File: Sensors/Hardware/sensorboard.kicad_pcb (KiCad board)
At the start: 4 copper layers, 120 x 50 mm, 302 parts, among them J1 RBUS, J10 1053131104, J11 1053131104, J12 1053131104, J13 1053131104, J14 1053131104, J15 USB_C_Receptacle_USB2.0, J16 Micro_SD_Card_Det, J2 Conn_Coaxial, J3 1053131104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

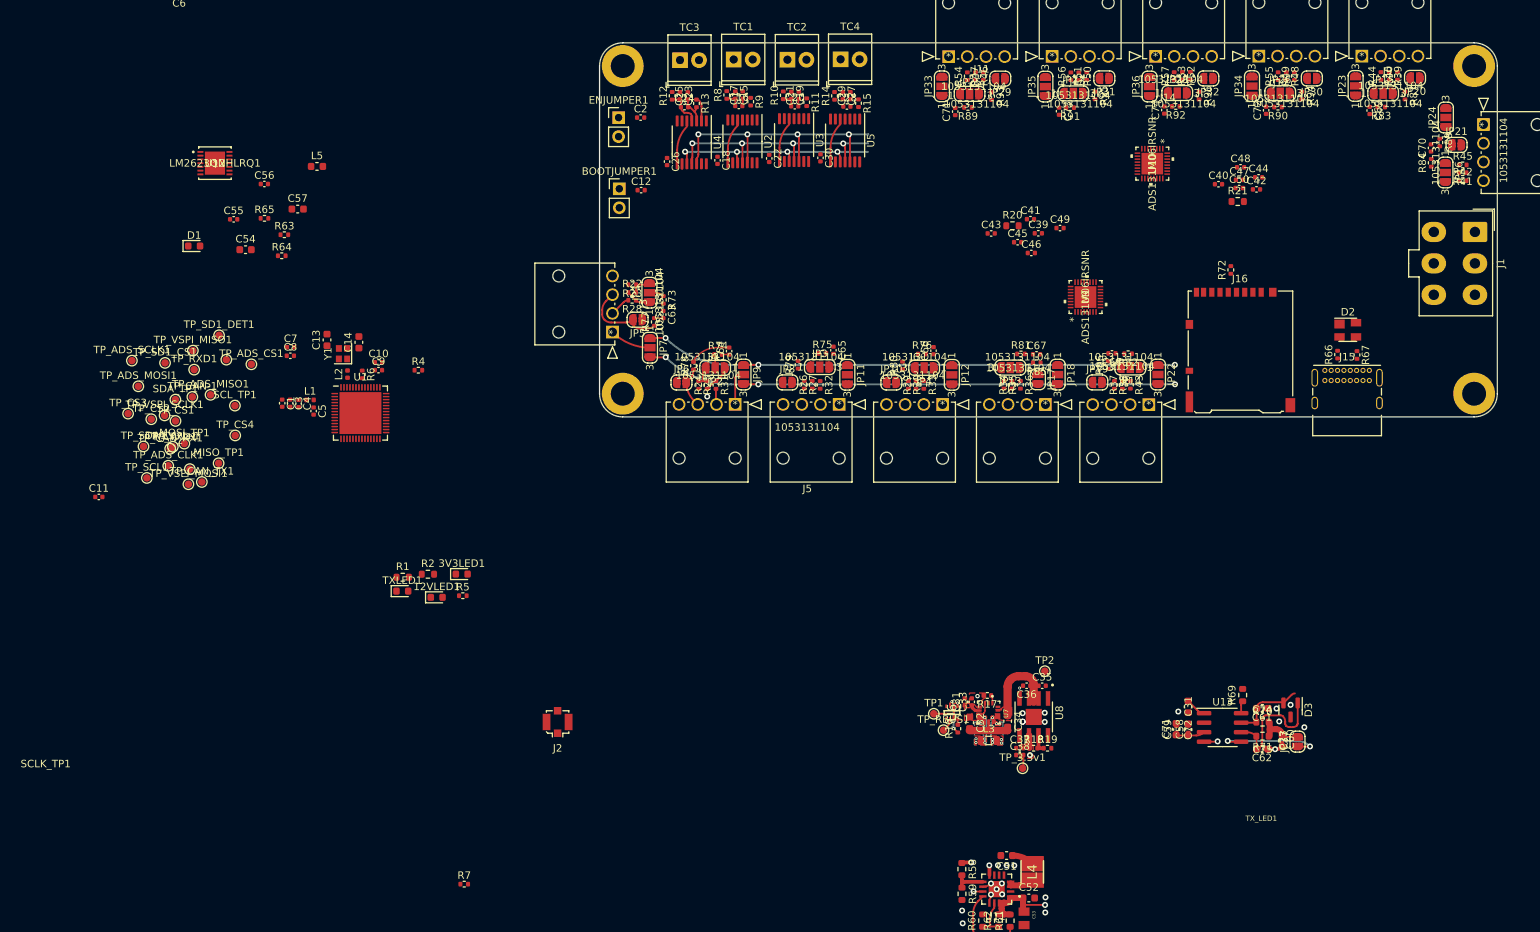
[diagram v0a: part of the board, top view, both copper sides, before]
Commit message: 10v rail layout, adc update
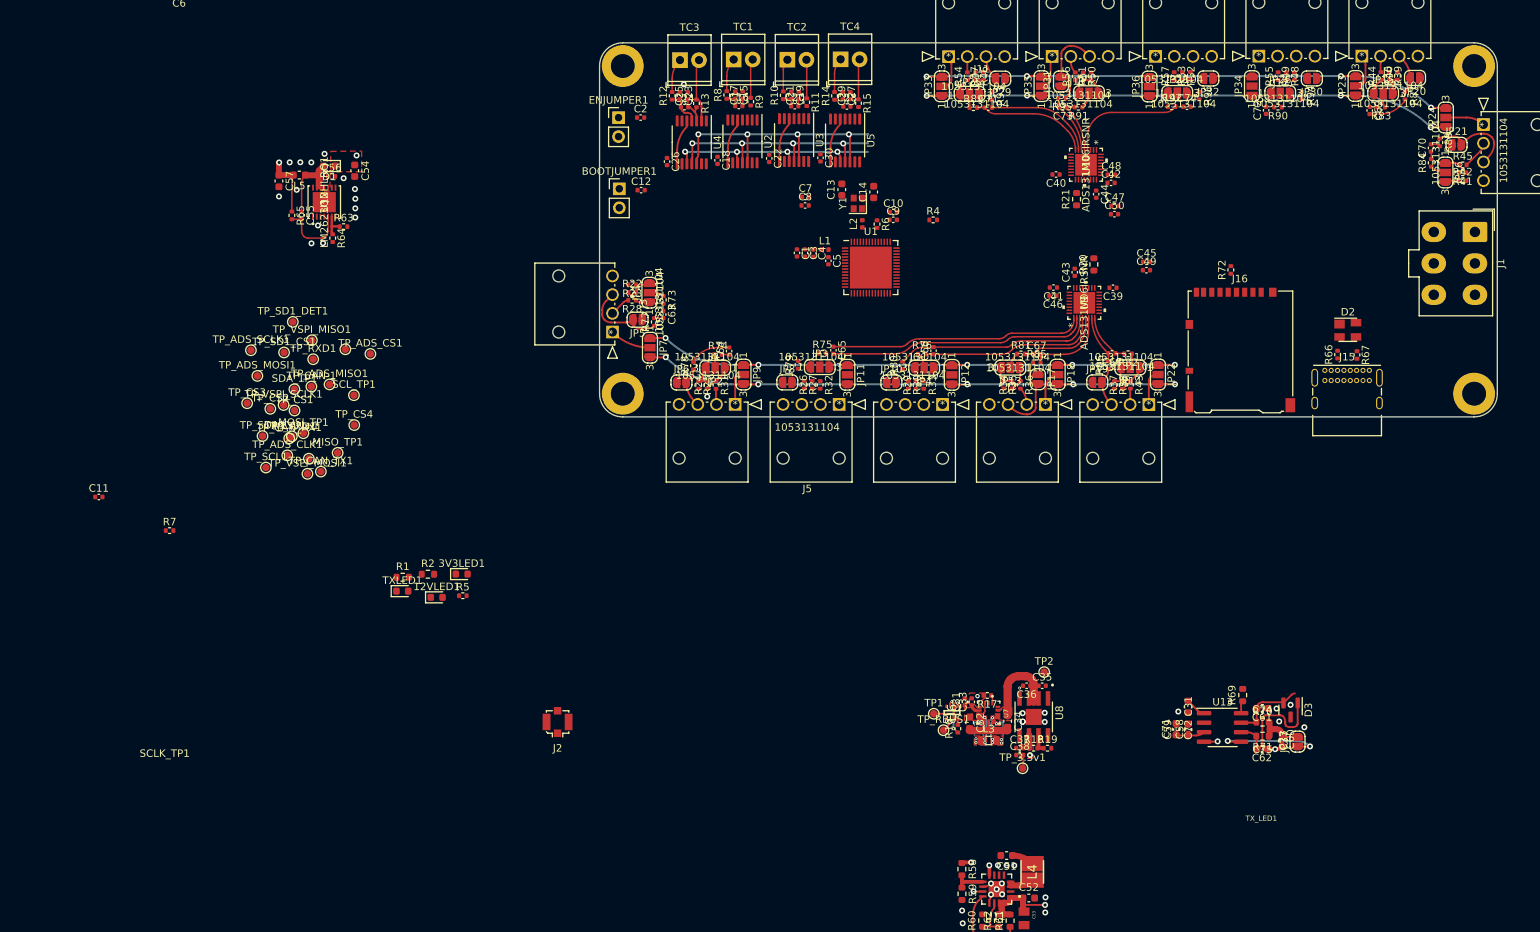
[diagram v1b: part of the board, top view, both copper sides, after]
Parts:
- moved C1 71.7 mm to (106.4, 58.1)
- moved C10 71.7 mm to (119.3, 52.6)
- moved C13 71.7 mm to (112.4, 49.6)
- moved C14 71.7 mm to (116.6, 49.9)
- moved C3 71.7 mm to (107.5, 58.1)
- moved C4 71.7 mm to (108.6, 58.1)
- moved C5 71.7 mm to (110.6, 59.1)
- moved C7 71.7 mm to (107.5, 50.6)
- moved C8 71.7 mm to (107.5, 51.7)
- moved C9 71.7 mm to (119.3, 53.7)
- moved L1 71.7 mm to (110.1, 57.6)
- moved L2 71.7 mm to (115.1, 54.2)
- moved R4 71.7 mm to (124.6, 53.7)
- moved R6 71.7 mm to (117.1, 54.2)
- moved Y1 71.7 mm to (114.5, 51.5)
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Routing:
- net +3V3: track 110.8 -> 202.1 mm, vias 7 -> 14
- net +5V: track 84.8 -> 167.7 mm, vias 4 -> 10
- net /analogueSPI/AIN2N: track 0.00 -> 34.8 mm
- net /analogueSPI/AIN2P: track 0.00 -> 33.9 mm
- net /analogueSPI/AIN3N: track 0.00 -> 26.8 mm
- net /analogueSPI/AIN3P: track 0.00 -> 23.9 mm
- net /analogueSPI/AIN11P: track 0.00 -> 15.8 mm
- net /analogueSPI/AIN11N: track 0.00 -> 15.7 mm
- net /analogueSPI/AIN9P: track 0.00 -> 15.6 mm
- net Net-(J10-Pad3): track 0.00 -> 12.2 mm
- net Net-(J13-Pad3): track 0.00 -> 11.7 mm
- net Net-(J7-Pad3): track 0.00 -> 11.5 mm
- net /analogueSPI/AIN4P: track 0.00 -> 11.4 mm
- net /analogueSPI/AIN4N: track 0.00 -> 11.3 mm
- net Net-(C55-Pad1): track 0.00 -> 9.82 mm
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- added copper zone on F.Cu, net +10V

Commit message: ADC update
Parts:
- moved JP8 5.43 mm to (110.5, 75.0), turned to -90 degrees
- moved JP30 5.38 mm to (169.8, 35.1), turned to 90 degrees
- moved R79 3.93 mm to (110.5, 72.7), turned to 0 degrees
- moved R94 3.80 mm to (170.1, 37.4), turned to 180 degrees
- moved JP3 2.62 mm to (106.8, 73.5), turned to 180 degrees
- moved JP26 2.46 mm to (173.4, 36.7)
- moved R90 1.41 mm to (172.1, 38.5)
- moved R75 1.32 mm to (108.5, 71.6)
- moved JP34 1.24 mm to (166.0, 35.8)
- moved JP11 1.22 mm to (114.3, 74.3)
- moved R26 1.18 mm to (107.2, 75.7)
- moved R27 1.18 mm to (106.2, 75.7)
- moved R32 1.18 mm to (108.3, 75.7)
- moved JP18 1.14 mm to (142.4, 74.4)
- moved C72 1.13 mm to (170.1, 38.4), turned to 180 degrees
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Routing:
- net /analogueSPI/AIN1P: track 0.99 -> 48.0 mm
- net /analogueSPI/AIN1N: track 5.52 -> 52.0 mm
- net /analogueSPI/AIN6P: track 1.01 -> 47.2 mm
- net /analogueSPI/AIN6N: track 1.24 -> 47.3 mm
- net /analogueSPI/AIN7P: track 1.04 -> 38.3 mm
- net /analogueSPI/AIN7N: track 5.46 -> 42.6 mm
- net /analogueSPI/AIN8P: track 0.00 -> 27.2 mm
- net /analogueSPI/AIN8N: track 0.00 -> 26.8 mm
- net /analogueSPI/AIN9N: track 0.00 -> 17.6 mm
- net Net-(J5-Pad3): track 0.00 -> 11.5 mm
- net Net-(J12-Pad3): track 0.00 -> 11.3 mm
- net Net-(J14-Pad3): track 0.00 -> 5.27 mm
- net Net-(J6-Pad3): track 0.00 -> 5.25 mm
- net Net-(J5-Pad1): track 0.00 -> 5.11 mm
- net Net-(J14-Pad1): track 0.00 -> 5.08 mm
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
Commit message: esp32 pin rearrangement
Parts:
- removed J2: Conn_Coaxial, Connector_Coaxial:U.FL_Molex_MCRF_73412-0110_Vertical
- moved C55 116.8 mm to (110.4, 146.3)
- moved C56 116.8 mm to (114.4, 141.2)
- moved R63 116.8 mm to (116.0, 147.9)
- moved R64 116.8 mm to (114.6, 149.4)
- moved R65 116.8 mm to (109.1, 146.4)
- moved U12 116.8 mm to (113.4, 144.6)
- moved C54 116.8 mm to (117.5, 140.4)
- moved C57 116.8 mm to (107.4, 141.8)
- moved D1 116.8 mm to (114.1, 139.8)
- moved L5 116.8 mm to (110.1, 141.0)
- moved C11 108.8 mm to (117.1, 58.7), turned to 90 degrees
- moved C31 100.8 mm to (213.9, 64.0)
- moved C32 100.8 mm to (214.6, 66.8)
- moved C33 100.8 mm to (214.9, 64.0)
- moved C34 100.8 mm to (219.7, 66.6)
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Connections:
- R20 pad 1: +3V3 -> Net-(R20-Pad1)
- R20 pad 2: Net-(R20-Pad2) -> +3V3
- U1 pad 12: /SDA -> unconnected-(U1-Pad12)
- U1 pad 13: /SCL -> unconnected-(U1-Pad13)
- U1 pad 23: /CS2 -> /CAN+
- U1 pad 27: /CS3 -> /CAN_TX
- U1 pad 28: /CS0 -> /CAN_RX
- U1 pad 36: /CAN_TX -> /MOSI
- U1 pad 37: /CAN_RX -> /MISO
- U1 pad 39: /MISO -> /CS2
- U1 pad 40: /SDA -> /CS1
- U1 pad 41: /SCL -> /CS0
- U1 pad 42: /MOSI -> /CS3
- U1 pad 43: /CS1 -> unconnected-(U1-Pad43)
- U1 pad 6: /CAN+ -> unconnected-(U1-Pad6)
- U9 pad 18: Net-(R20-Pad2) -> Net-(R20-Pad1)
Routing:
- net VBUS: track 5.27 -> 18.3 mm
- net /Data-: track 0.00 -> 7.34 mm
- net /Data+: track 0.00 -> 6.76 mm
- net Net-(R68-Pad2): track 0.00 -> 1.26 mm
- net (no net): vias 25 -> 26
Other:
- board text added: "CS regular spi"
- board text added: "Immoveable: DATA +- unavailable pins: 1,4,8,5,2,3,20,30-35,46,52,53,54,56,55,"
- board text added: "POwer circuits just require 3.3V etc. Therefore can be put into the left or right side of the board"
- board text added: "VSPI spi (microSD) CAN TX and RX, CAN +- DAta + and -"

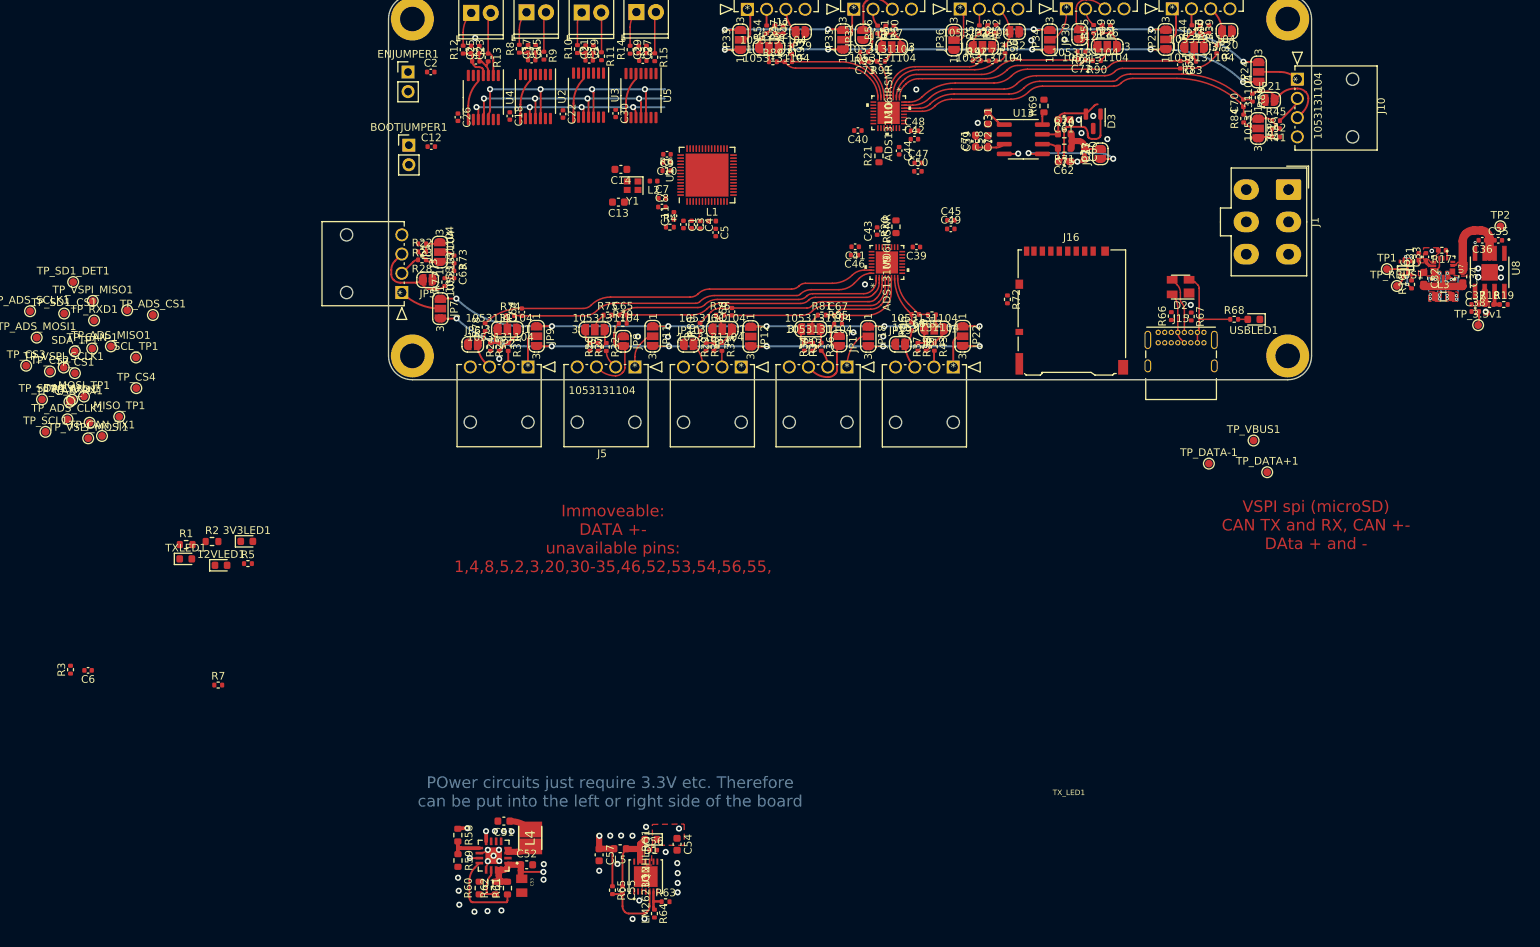
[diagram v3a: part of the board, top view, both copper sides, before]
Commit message: esp32-s3 placement
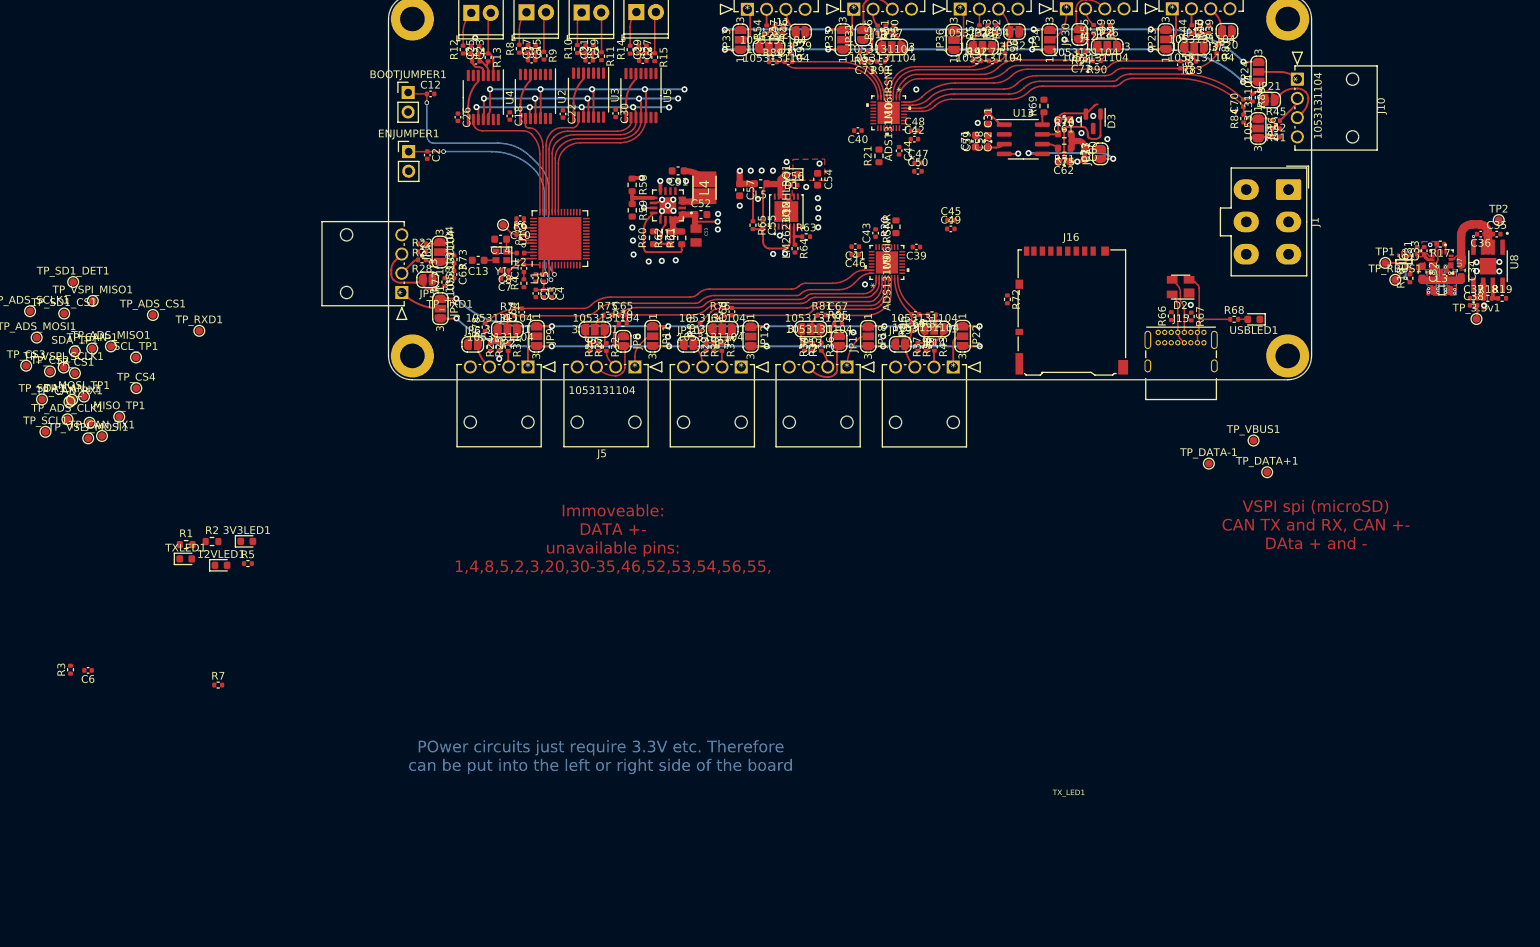
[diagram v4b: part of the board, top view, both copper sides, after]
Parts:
- moved R63 88.4 mm to (134.3, 61.4)
- moved R65 88.4 mm to (127.4, 59.9)
- moved C55 88.4 mm to (128.7, 59.9)
- moved C56 88.4 mm to (132.7, 54.7)
- moved R64 88.4 mm to (132.8, 62.9)
- moved U12 88.4 mm to (131.7, 58.1)
- moved C54 88.4 mm to (135.8, 53.9)
- moved C57 88.4 mm to (125.7, 55.3)
- moved D1 88.4 mm to (132.4, 53.3)
- moved L5 88.4 mm to (128.4, 54.5)
- moved U11 87.5 mm to (116.3, 57.3)
- moved C51 87.5 mm to (117.7, 52.9)
- moved C52 87.5 mm to (120.6, 58.5)
- moved C53 87.5 mm to (120.0, 61.2)
- moved L4 87.5 mm to (121.1, 55.0)
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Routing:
- net /BOOT: track 0.00 -> 40.0 mm, vias 0 -> 2
- net /CHIP_PU: track 0.00 -> 33.8 mm, vias 0 -> 2
- net /MOSI: track 37.9 -> 61.5 mm, vias 4 -> 5
- net /MISO: track 33.9 -> 56.8 mm, vias 4 -> 5
- net /SCLK: track 30.6 -> 52.5 mm, vias 4 -> 5
- net /CS2: track 0.00 -> 21.3 mm
- net /CS3: track 0.69 -> 19.1 mm
- net /CS1: track 0.00 -> 15.3 mm
- net /CS0: track 0.00 -> 13.4 mm
- net +3V3: track 206.6 -> 216.8 mm
- net Net-(C14-Pad1): track 0.00 -> 2.97 mm
- net Net-(C5-Pad1): track 0.00 -> 2.27 mm
- net Net-(R6-Pad1): track 0.00 -> 2.20 mm
- net Net-(TP_RXD1-Pad1): track 0.00 -> 2.19 mm, vias 0 -> 1
- net Net-(C11-Pad2): track 0.00 -> 2.09 mm
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
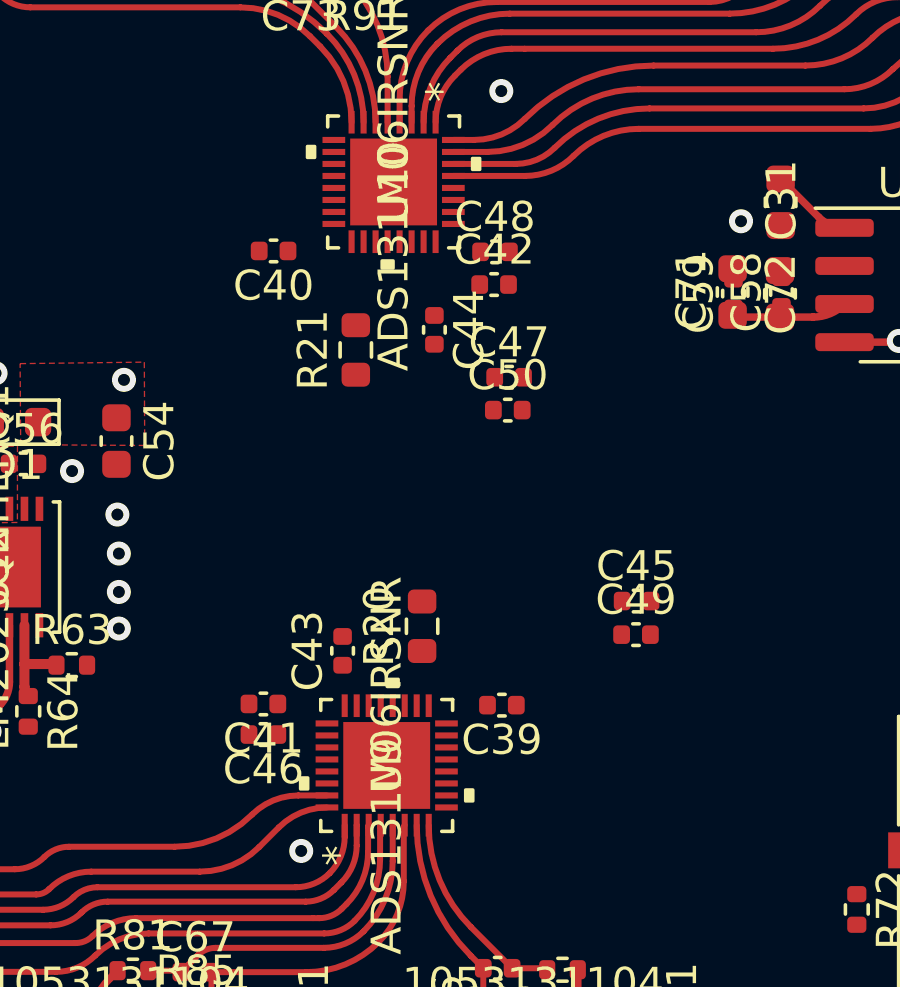
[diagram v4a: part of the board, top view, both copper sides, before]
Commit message: ADC SPI connections
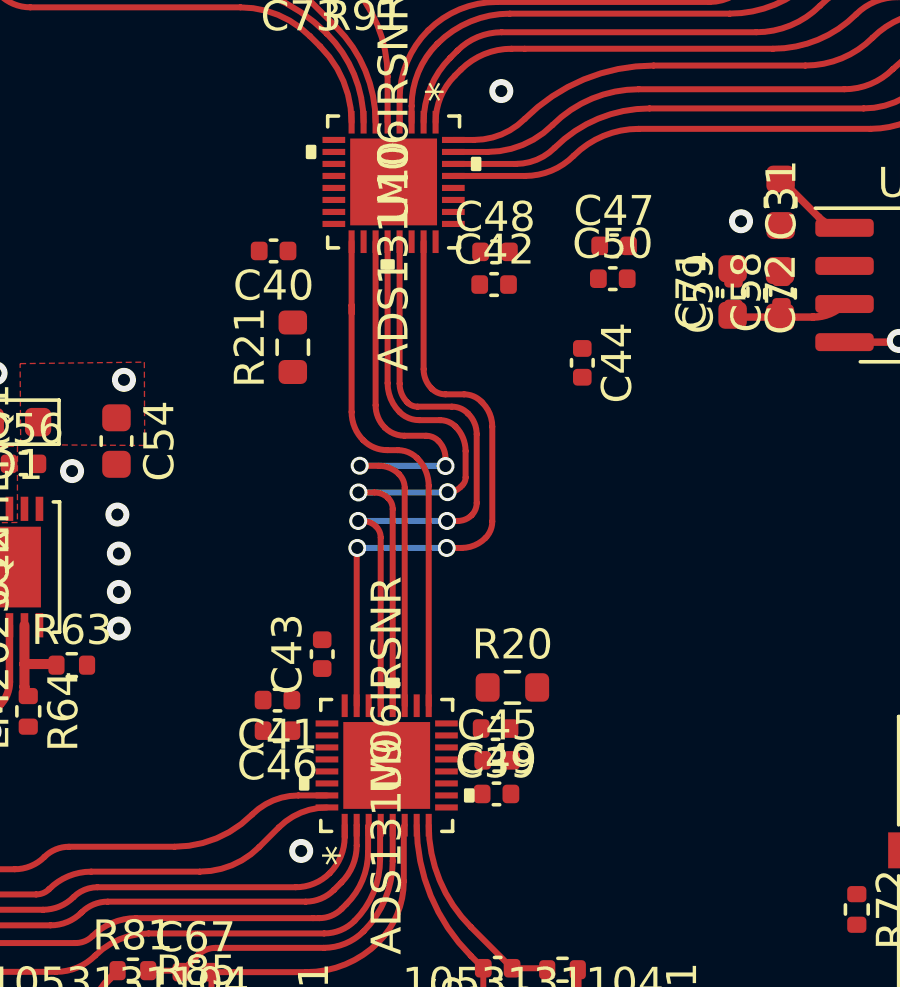
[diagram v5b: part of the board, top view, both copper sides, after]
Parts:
- moved C49 7.06 mm to (148.4, 65.7)
- moved C45 7.06 mm to (148.5, 64.6)
- moved C47 5.61 mm to (152.4, 47.4)
- moved C50 5.61 mm to (152.3, 48.5)
- moved C44 5.05 mm to (151.3, 51.3)
- moved R20 3.64 mm to (149.0, 62.1), turned to 0 degrees
- moved R21 2.10 mm to (141.7, 50.8)
- moved C39 0.81 mm to (148.4, 63.5)
- moved C43 0.69 mm to (142.6, 61.0)
- moved C41 0.49 mm to (141.2, 62.6)
- moved C46 0.49 mm to (141.2, 63.6)
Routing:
- net /ADS_MOSI: track 0.00 -> 21.6 mm, vias 0 -> 2
- net /ADS_MISO: track 0.00 -> 21.4 mm, vias 0 -> 2
- net /ADS_SCLK: track 0.00 -> 21.1 mm, vias 0 -> 2
- net /ADS_CLK: track 1.34 -> 22.4 mm, vias 1 -> 3
- net /ADS_CS: track 0.00 -> 17.3 mm
